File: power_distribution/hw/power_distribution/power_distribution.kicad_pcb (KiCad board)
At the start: 4 copper layers, 95.9 x 35.1 mm, 78 parts, among them J1 XT30-M_Ver, J2 JST-PH_01x02, J3 JST-PH_01x02, J4 JST-PH_01x02, J5 JST-PH_01x02, Q1 60Vds, U1 LMR51635XFDDCR, U2 AP63205WU-7, U3 AP63203WU-7

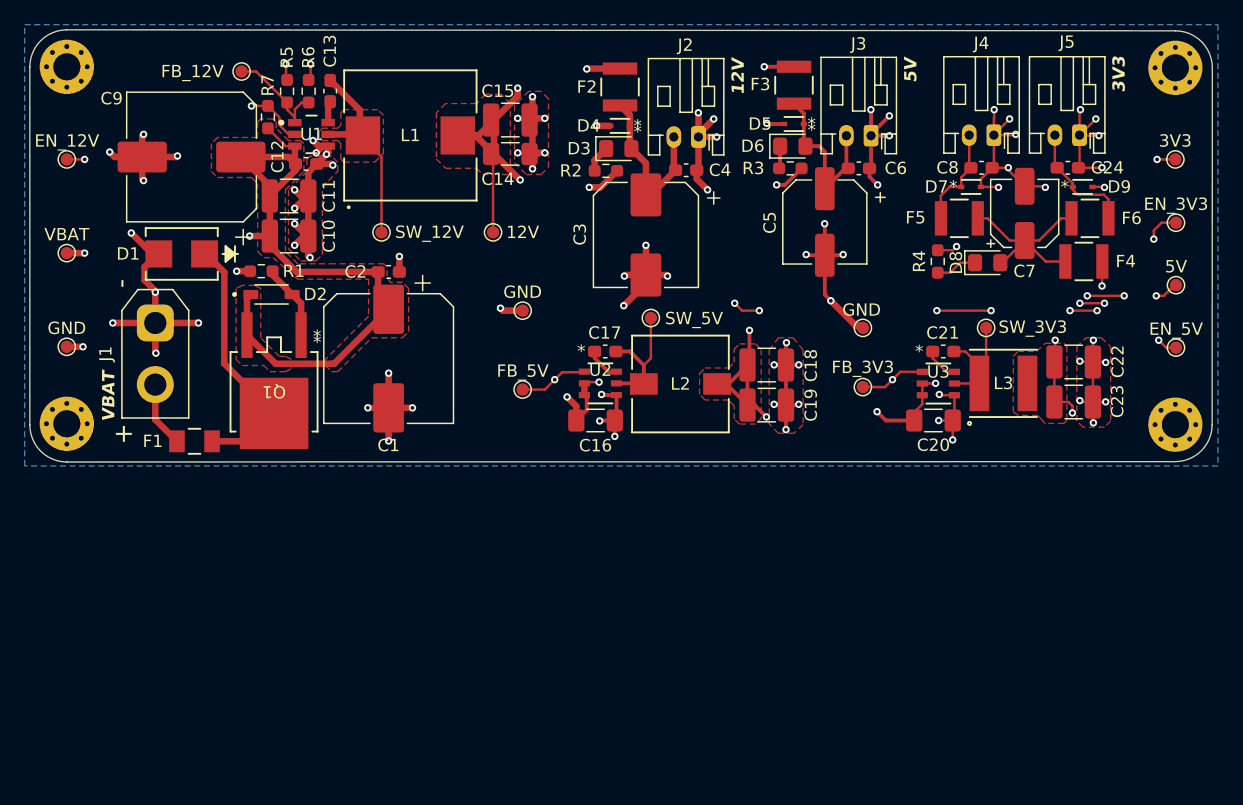
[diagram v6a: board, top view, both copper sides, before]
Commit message: Updated BOM. Ordered parts!
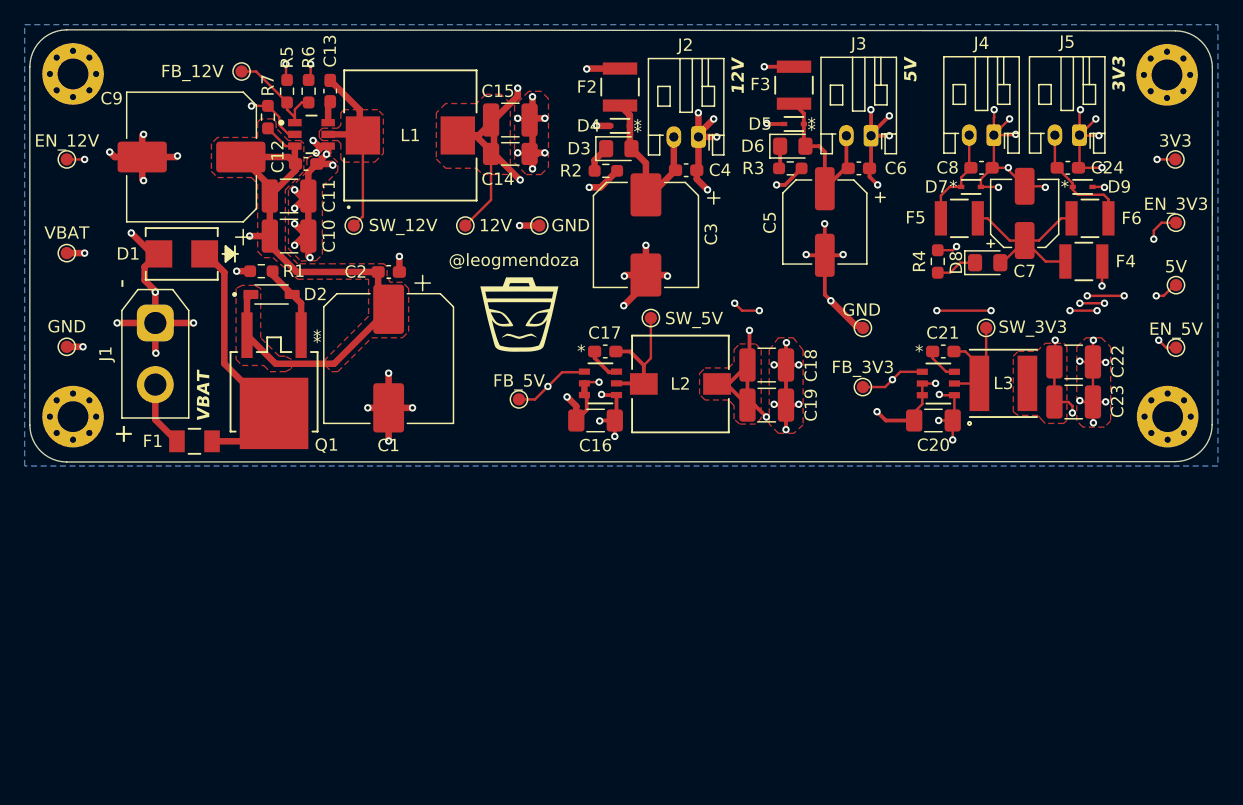
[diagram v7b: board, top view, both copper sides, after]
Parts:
- added G***: LOGO, LOGO, F.Cu at (51.7, 35.1)
- added G***: LOGO, LOGO, B.Cu at (59.9, 24.7)
- H1, H2, H3, H4: footprint MountingHole:MountingHole_2.2mm_M2_Pad_Via -> MountingHole:MountingHole_2.5mm_Pad_Via
- moved GND2 7.03 mm to (53.4, 27.9)
- moved 12V1 2.32 mm to (47.4, 27.9)
- moved SW_12V1 2.32 mm to (38.3, 27.9)
- moved H4 0.90 mm to (104.3, 43.4)
- moved H2 0.89 mm to (104.3, 15.7)
- moved FB_5V1 0.85 mm to (51.7, 42.0)
- moved H1 0.77 mm to (15.5, 15.6)
- moved H3 0.77 mm to (15.5, 43.4)
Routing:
- net GND: track 190.5 -> 189.5 mm
- net Net-(U1-SW): track 16.7 -> 15.7 mm
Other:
- board text added: "*"
- board text added: "@leogmendoza"
- board text added: "Power Distribution Board v1 for F25 Skateboard by Leopoldo Mendoza"
